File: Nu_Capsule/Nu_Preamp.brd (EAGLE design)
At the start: 9.4 x 14.8 mm, 20 parts, among them T1 2SC3324, T2 2SC3324

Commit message: Updated files for version 2.0
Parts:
- removed C5: 4.7uF, resistor:C0603
- removed H2: 3P-2MM-TH-MALE, CYCFI_Con:3P-2MM-TH
- removed PAD18, PAD19, PAD6, PAD7: WIREPADSMD1,27-254, wirepad:SMD1,27-2,54
- removed R7: 4.7K, resistor:R0402
- removed T1, T2: 2SC3324, transistor:SOT23
- added D1: (no value), m-pad-2.1:SOD-323
- added IC, OC: (no value), wirepad:1,6/0,8
- added U1: OPA209AIDVBR, CYCFI_semicon:SOT23-5
- C1: value 4.7uF -> 100pF, 25V; device resistor:C0603 -> rcl:C0402
- C2: value 100pF -> 4.7uF, 25V; device resistor:C0603 -> rcl:C0603_NK
- C3: value 4.7uF -> 0.1uF, 25V; device resistor:C0603 -> rcl:C0402
- C4: value 0.1uf -> 4.7uF, 25V; device resistor:C0603 -> rcl:C0603
- H1: value 2P-2MM-TH-MALE -> 4P_ZIF_59453-041110EDHLF; device CYCFI_Con:2P-2MM-TH -> CYCFI_Con:4P_ZIF_59453-041110EDHLF
- R1: value 200K -> 1.2K; device resistor:R0603 -> resistor:R0402
- R2: value 52.3K -> 1.2K
- R3: value 330 -> 22K
- R4: value 22K -> 47K
- R5: value 10K -> 47K
- moved R5 8.72 mm to (7.54, 11.5), flipped to the bottom
- moved C3 8.36 mm to (5.19, 11.5), flipped to the bottom, turned to 0 degrees
- moved H1 8.10 mm to (5.19, 5.74), flipped to the bottom, turned to 0 degrees
- moved C1 7.90 mm to (6.63, 3.49), turned to 0 degrees
- moved R1 6.60 mm to (2.17, 5.81), flipped to the bottom
- moved R3 5.74 mm to (2.78, 12.6), flipped to the bottom, turned to 90 degrees
- moved R2 5.74 mm to (8.05, 5.83), flipped to the bottom, turned to 90 degrees
- moved C2 3.96 mm to (5.17, 10.4), flipped to the bottom, turned to 0 degrees
- moved R6 2.25 mm to (5.23, 1.94), turned to 180 degrees
- moved R4 1.95 mm to (5.16, 13.7)
- moved C4 1.80 mm to (3.46, 3.46), turned to 180 degrees
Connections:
- removed net N$3: C5.2, R5.2, T2.2
- removed net OUTPUT: H1.P$1, R7.2
- removed net VCVF: R1.2, R4.1, T1.3, T2.1
- removed net VIN: C3.2, C4.2, H2.P$1, R4.2, T2.3
- new net N$5: C4.1, R3.2, U1.1
- new net N$6: R1.2, R4.1, R5.2, U1.3
- new net N$7: R2.2, R3.1, U1.4
- new net VCC: C2.2, C3.2, D1.2, R5.1, U1.5
- net GND: now also H1.P$3, R4.2, U1.2; no longer C4.1, H2.P$2, H2.P$3, PAD7.1, R2.1, R3.1, R5.1
- net N$1: now also D1.1, H1.P$1; no longer C1.2, R1.1, R2.2, T1.1
- net N$2: now also IC.1, R1.1; no longer C2.2, PAD6.1
- net N$4: now also C1.2, OC.1, R2.1; no longer R3.2, T1.2
- net OUT: now also C4.2, H1.P$4; no longer C5.1, R7.1
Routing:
- net GND: track 44.2 -> 10.9 mm, vias 3 -> 4
- net VIN: track 24.8 -> 0.00 mm, vias 3 -> 0
- net VCVF: track 17.1 -> 0.00 mm, vias 3 -> 0
- net N$6: track 0.00 -> 16.8 mm, vias 0 -> 4
- net N$5: track 0.00 -> 16.0 mm, vias 0 -> 1
- net N$7: track 0.00 -> 15.6 mm, vias 0 -> 2
- net VCC: track 0.00 -> 9.26 mm, vias 0 -> 2
- net OUTPUT: track 7.71 -> 0.00 mm, vias 1 -> 0
- net N$1: track 8.47 -> 1.80 mm
- net N$3: track 5.40 -> 0.00 mm
- net OUT: track 5.83 -> 10.6 mm, vias 0 -> 1
- net N$4: track 2.02 -> 6.26 mm, vias 0 -> 1
- net N$2: track 4.88 -> 9.05 mm
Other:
- board size 9.4 x 14.8 mm -> 8.9 x 17 mm
- board text removed: "C1"
- board text removed: "C2"
- board text removed: "C3"
- board text removed: "C4"
- board text removed: "C5"
- board text removed: "CYCFI 2016"
- board text removed: "H1"
- board text removed: "H2"
- board text removed: "IC"
- board text removed: "Nu v1.5"
- board text removed: "O"
- board text removed: "OC"
- board text removed: "R1"
- board text removed: "R2"
- board text removed: "R3"
- board text removed: "R4"
- board text removed: "R5"
- board text removed: "R6"
- board text removed: "R7"
- board text removed: "T1"
- board text removed: "T2"
- board text removed: "V+"
- board text removed: "V-"

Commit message: Updated Nu Preamp Files
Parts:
- removed C4: 4.7uF, 25V, rcl:C0603
- removed IC, OC: (no value), wirepad:1,6/0,8
- removed R1: 1.2K, resistor:R0402
- added H2: 3P-2MM-TH-MALE, CYCFI_Con:3P-2MM-TH
- added Q1, Q2: 2SC3324, CYCFI_semicon:SOT23
- added R10, R11: 1.2k, rcl:R0402
- added R12: 12k, rcl:R0402
- added R13, R15: 100k, rcl:R0402
- added R14, R16: 51k, rcl:R0402
- added R7: 150k, resistor:R0402
- added R8, R9: 33k, rcl:R0402
- C1: value 100pF, 25V -> 0.1uF, 25V
- C3: value 0.1uF, 25V -> 10uF, 25V; device rcl:C0402 -> rcl:C0603_NK
- H1: value 4P_ZIF_59453-041110EDHLF -> 2P-2MM-TH-MALE; device CYCFI_Con:4P_ZIF_59453-041110EDHLF -> CYCFI_Con:2P-2MM-TH
- R2: value 1.2K -> 10k; device resistor:R0402 -> rcl:R0402
- R3: value 22K -> 75k
- R4, R5: value 47K -> 33k
- R6: value 10K -> 150k
- U1: value OPA209AIDVBR -> TLV170
- moved C3 9.86 mm to (2.50, 2.01), flipped to the top
- moved U1 9.75 mm to (5.70, 4.66), flipped to the top, turned to 0 degrees
- moved R4 8.24 mm to (8.34, 6.08)
- moved R3 7.95 mm to (2.10, 4.67), flipped to the top
- moved R2 6.48 mm to (2.50, 2.48), turned to 0 degrees
- moved C2 6.03 mm to (3.40, 4.60), flipped to the top, turned to 90 degrees
- moved D1 6.00 mm to (4.08, 14.8), turned to 180 degrees
- moved H1 4.20 mm to (5.98, 1.61), flipped to the top
- moved R5 4.12 mm to (8.10, 7.43), flipped to the top, turned to 0 degrees
- moved C1 4.10 mm to (5.07, 7.29)
- moved R6 1.72 mm to (5.82, 3.56), flipped to the bottom
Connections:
- removed net N$2: C1.1, IC.1, R1.1
- removed net N$4: C1.2, OC.1, R2.1
- removed net N$7: R2.2, R3.1, U1.4
- removed net OUT: C4.2, H1.P$4, R6.2
- removed net VCC: C2.2, C3.2, D1.2, R5.1, U1.5
- new net IN+: Q1.1, R13.1, R14.2
- new net IN-: Q2.1, R15.1, R16.2
- new net N$10: Q2.2, R11.2
- new net N$13: R10.1, R11.1, R12.2
- new net N$14: R5.2, R6.1, R7.2, U1.3
- new net N$15: R3.2, R4.2, U1.4
- new net N$16: C3.1, R3.1, U1.1
- new net N$19: D1.1, H2.P$1
- new net N$9: Q1.2, R10.2
- new net VCC1: C1.1, C2.2, D1.2, R13.2, R15.2, R7.1, R8.2, R9.2, U1.5
- net GND: now also C1.2, H2.P$2, H2.P$3, R12.1, R14.1, R16.1, R2.1, R6.2; no longer C3.1, H1.P$3, R4.2, R6.1
- net N$1: now also C3.2, R2.2; no longer D1.1
- net N$5: now also Q1.3, R5.1, R8.1; no longer C4.1, R3.2, U1.1
- net N$6: now also Q2.3, R9.1; no longer R1.2, R5.2, U1.3
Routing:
- net VCC1: track 0.00 -> 30.6 mm, vias 0 -> 2
- net IN-: track 0.00 -> 16.1 mm, vias 0 -> 2
- net N$7: track 15.6 -> 0.00 mm, vias 2 -> 0
- net N$6: track 16.8 -> 5.47 mm, vias 4 -> 0
- net OUT: track 10.6 -> 0.00 mm, vias 1 -> 0
- net N$14: track 0.00 -> 10.3 mm, vias 0 -> 1
- net VCC: track 9.26 -> 0.00 mm, vias 2 -> 0
- net N$2: track 9.05 -> 0.00 mm, vias 1 -> 0
- net GND: track 10.9 -> 3.36 mm, vias 4 -> 3
- net N$15: track 0.00 -> 6.91 mm
- net N$16: track 0.00 -> 6.42 mm
- net N$4: track 6.26 -> 0.00 mm, vias 1 -> 0
- net N$10: track 0.00 -> 5.59 mm
- net IN+: track 0.00 -> 5.12 mm, vias 0 -> 1
- net N$1: track 1.80 -> 6.57 mm
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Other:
- board size 8.9 x 17 mm -> 10 x 18 mm
- board text added: "GND"
- board text added: "O"
- board text added: "V+"

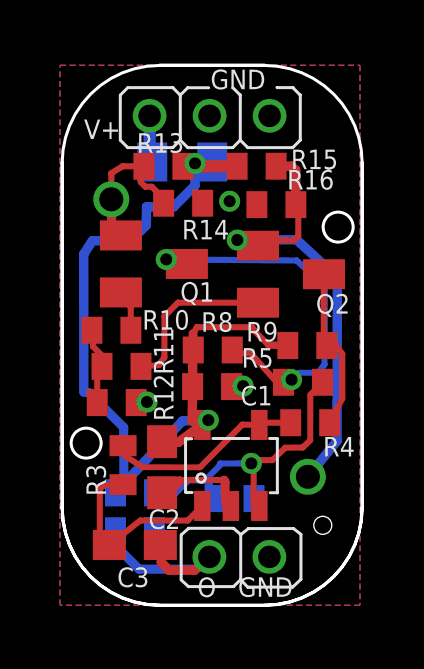
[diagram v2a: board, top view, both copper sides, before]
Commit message: Updated files for Nu Preamp v2.1.1 added
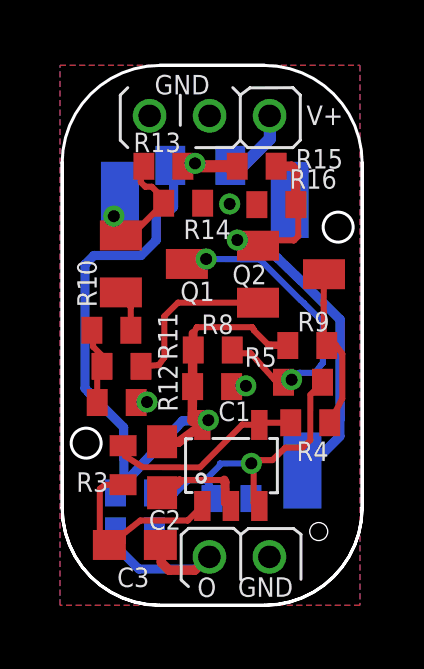
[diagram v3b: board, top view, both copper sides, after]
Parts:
- added GND, IN+, IN-: (no value), wirepad:SMD1,27-2,54
- moved D1 0.61 mm to (4.68, 14.7), turned to 0 degrees
- moved R6 0.10 mm to (5.71, 3.56)
- turned H2 to 180 degrees
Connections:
- net GND: now also GND.1
- net IN+: now also IN+.1
- net IN-: now also IN-.1
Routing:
- net N$5: track 13.2 -> 11.4 mm
- net N$19: track 1.58 -> 2.54 mm
- net IN-: track 16.1 -> 15.4 mm, vias 2 -> 1
- net VCC1: track 30.6 -> 30.0 mm

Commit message: Remove commas and voltage rating on capacitor symbols on schematics
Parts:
- C1: value 0.1uF, 25V -> 0.1uF
- C2: value 4.7uF, 25V -> 4.7uF
- C3: value 10uF, 25V -> 10uF
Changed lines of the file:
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@@
 <attribute name="VALUE" x="6.44575" y="12.65075" size="1.27" layer="28" rot="MR0"/>
 </element>
-<element name="C1" library="rcl" package="C0402" value="0.1uF, 25V" x="5.07" y="7.29" smashed="yes">
+<element name="C1" library="rcl" package="C0402" value="0.1uF" x="5.07" y="7.29" smashed="yes">
 <attribute name="NAME" x="5.2785" y="6.14025" size="0.65" layer="25" font="vector" ratio="13"/>
 <attribute name="VALUE" x="4.435" y="5.385" size="0.65" layer="27"/>
@@
 </element>
 <element name="U1" library="CYCFI_semicon" package="SOT23-5" value="TLV170" x="5.695" y="4.66" smashed="yes"/>
-<element name="C3" library="rcl" package="C0603_NK" value="10uF, 25V" x="2.495" y="2.01" smashed="yes">
+<element name="C3" library="rcl" package="C0603_NK" value="10uF" x="2.495" y="2.01" smashed="yes">
 <attribute name="NAME" x="1.905" y="0.6075" size="0.65" layer="25" font="vector" ratio="13"/>
 <attribute name="VALUE" x="1.86" y="0.105" size="0.65" layer="27"/>
@@
 <element name="H2" library="CYCFI_Con" package="3P-2MM-TH" value="3P-2MM-TH-MALE" x="4.9875" y="16.315" smashed="yes" rot="R180"/>
 <element name="H1" library="CYCFI_Con" package="2P-2MM-TH" value="2P-2MM-TH-MALE" x="5.98" y="1.6125" smashed="yes"/>
-<element name="C2" library="rcl" package="C0603_NK" value="4.7uF, 25V" x="3.4025" y="4.6025" smashed="yes" rot="R90">
+<element name="C2" library="rcl" package="C0603_NK" value="4.7uF" x="3.4025" y="4.6025" smashed="yes" rot="R90">
 <attribute name="NAME" x="4.03025" y="3.1695" size="0.65" layer="25" font="vector" ratio="13" rot="R180"/>
 <attribute name="VALUE" x="5.3075" y="3.9675" size="0.65" layer="27" rot="R90"/>
